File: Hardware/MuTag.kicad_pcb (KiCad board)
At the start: 2 copper layers, 30 x 20 mm, 32 parts, among them IC1 ST25DV04K-IER6S3, J1 Conn_01x02, J2 Conn_01x04, J3 Conn_01x06, U1 STM8

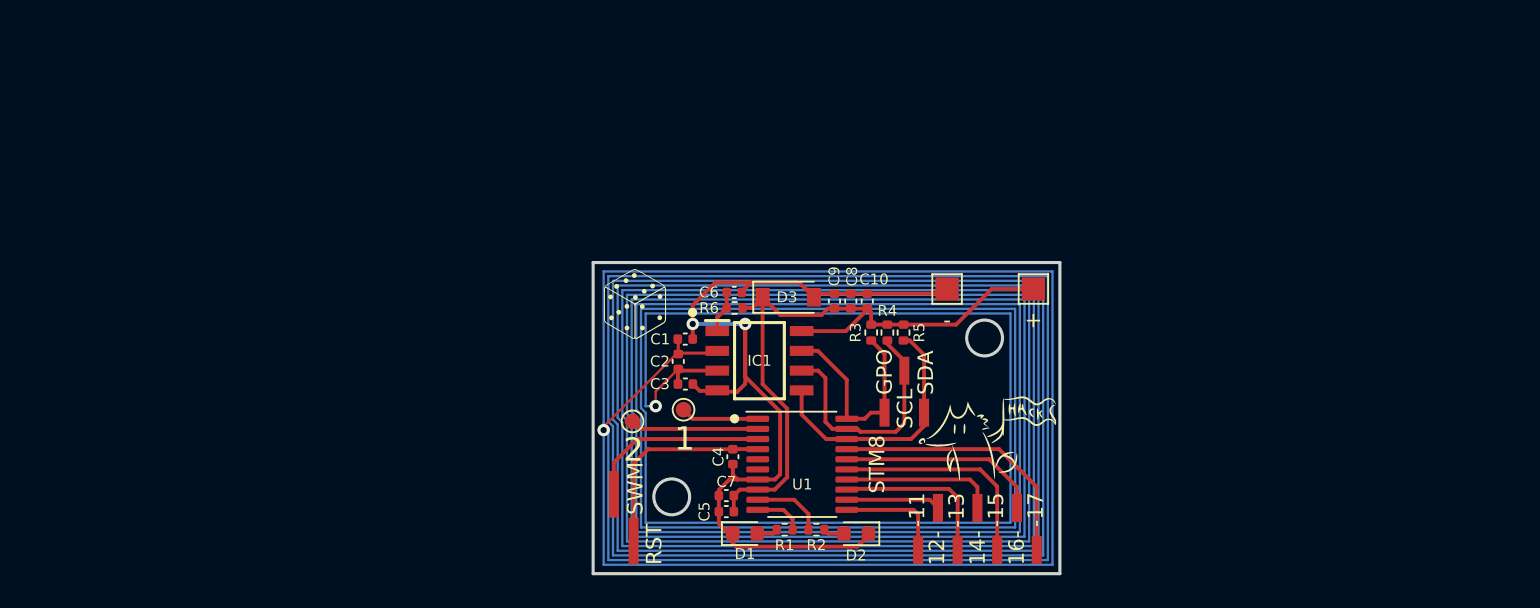
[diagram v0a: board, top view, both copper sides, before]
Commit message: First routing of new version - no antenna
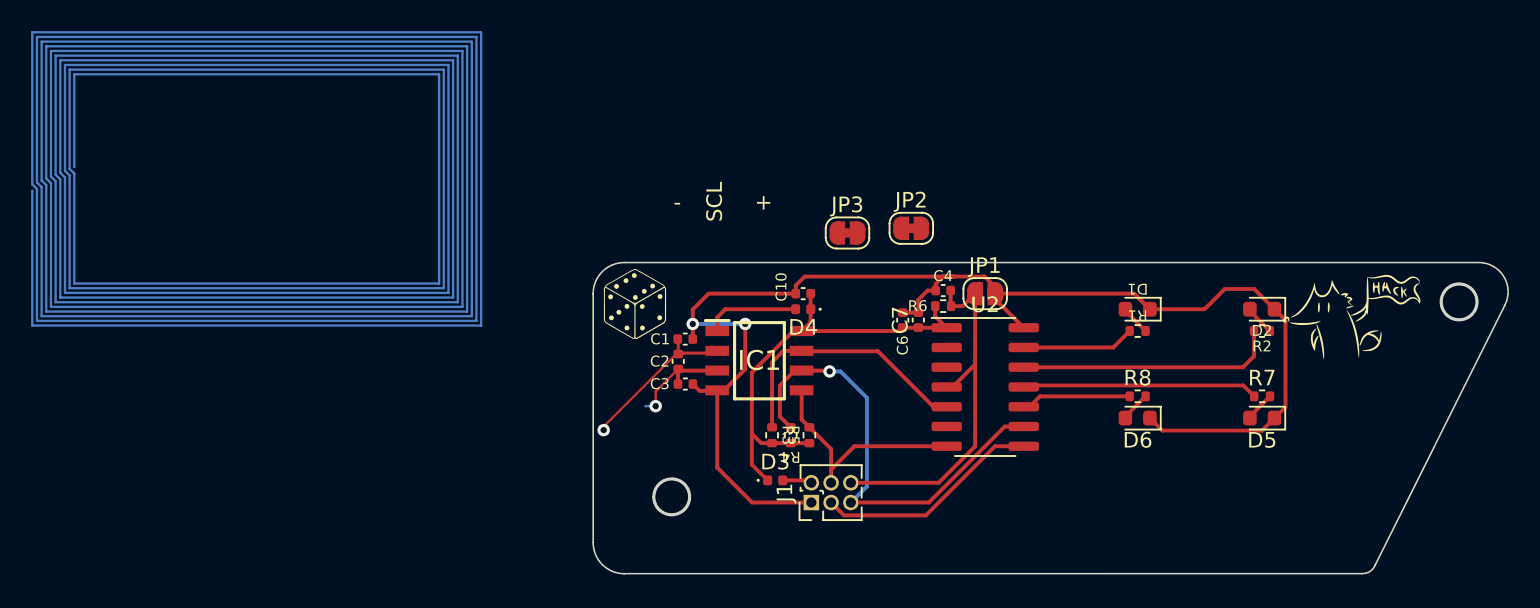
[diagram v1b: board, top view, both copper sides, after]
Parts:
- removed C5: 1uF, Capacitor_SMD:C_0402_1005Metric
- removed C8: 4.7uF, Capacitor_SMD:C_0402_1005Metric
- removed C9: 100nF, Capacitor_SMD:C_0402_1005Metric
- removed J2: Conn_01x04, Connector_PinHeader_1.27mm:PinHeader_1x02_P1.27mm_Vertical_SMD_Pin1Right
- removed J3: Conn_01x06, Connector_PinSocket_1.27mm:PinSocket_1x07_P1.27mm_Vertical_SMD_Pin1Right
- removed TP1, TP2: TestPoint, TestPoint:TestPoint_Pad_1.5x1.5mm
- removed TP3, TP4: TestPoint, TestPoint:TestPoint_Pad_D1.0mm
- removed U1: STM8, Package_SO:TSSOP-20_4.4x6.5mm_P0.65mm
- added D4: D, Diode_SMD:D_0402_1005Metric, F.Cu at (43.5, 23.0)
- added D5: LED, LED_SMD:LED_0603_1608Metric, F.Cu at (73.0, 30.0)
- added D6: LED, LED_SMD:LED_0603_1608Metric, F.Cu at (65.0, 30.0)
- added JP1: RESET_JMP, Jumper:SolderJumper-2_P1.3mm_Open_RoundedPad1.0x1.5mm, F.Cu at (55.2, 22.0)
- added JP2: SCL_JMP, Jumper:SolderJumper-2_P1.3mm_Bridged_RoundedPad1.0x1.5mm, F.Cu at (50.5, 17.8)
- added JP3: SDA_JMP, Jumper:SolderJumper-2_P1.3mm_Bridged_RoundedPad1.0x1.5mm, F.Cu at (46.4, 18.1)
- added R7: 220, Resistor_SMD:R_0402_1005Metric, F.Cu at (73.0, 28.6)
- added R8: 220, Resistor_SMD:R_0402_1005Metric, F.Cu at (65.0, 28.6)
- added U2: ATtiny24A-SS, Package_SO:SOIC-14_3.9x8.7mm_P1.27mm, F.Cu at (55.2, 28.0)
- C6: value 10nF -> 100nF
- C7: value 100nF -> 1nF
- D3: value D_Zener -> D; footprint Diode_SMD:D_SOD-123 -> Diode_SMD:D_0402_1005Metric
- J1: value Conn_01x02 -> SPI_Header; footprint Connector_PinSocket_1.27mm:PinSocket_1x03_P1.27mm_Vertical_SMD_Pin1Right -> Connector_PinHeader_1.27mm:PinHeader_2x03_P1.27mm_Vertical
- R1, R2: value 1.5K -> 220
- R3: value 20K -> 1.5K
- R6: value 200 -> 4.7K
- moved A1 39.8 mm to (22.9, 24.1)
- moved R2 31.4 mm to (73.0, 24.4)
- moved D2 29.8 mm to (73.0, 23.0)
- moved D1 29.1 mm to (65.0, 23.0), turned to 180 degrees
- moved R1 26.0 mm to (65.0, 24.4), turned to 180 degrees
- moved G*** 24.7 mm to (78.8, 23.5)
- moved C4 17.2 mm to (52.5, 21.8), turned to 180 degrees
- moved C7 16.7 mm to (50.9, 23.7), turned to 90 degrees
- moved G*** 15.0 mm to (60.0, 30.0)
- moved R6 13.4 mm to (52.5, 22.8)
- moved D3 11.8 mm to (41.7, 34.0)
- moved C6 11.0 mm to (49.9, 23.7), turned to 90 degrees
- moved J1 9.30 mm to (44.0, 35.4), turned to 90 degrees
- moved R3 9.17 mm to (41.5, 31.1), turned to 90 degrees
- moved R4 9.06 mm to (42.7, 31.1), turned to 90 degrees
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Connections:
- C4 pad 1: /MCU_RESET -> /RESET
- C6 pad 1: /NFC_V_EH -> VCC
- D3 pad 2: GND -> VDD
- IC1 pad 5: /NFC_SDA -> /SDA/MOSI
- IC1 pad 6: /NFC_SCL -> /SCL/SCK
- IC1 pad 7: /NFC_GPO -> /INT0
- J1 pad 1: /NFC_SDA -> GND
- J1 pad 2: /NFC_SCL -> VDD
- J1 pad 3: /NFC_GPO -> /MISO
- R2 pad 1: /LED_BLU -> /LED_BLUE
- R3 pad 2: /NFC_GPO -> /INT0
- R4 pad 2: /NFC_SCL -> /SCL/SCK
- R5 pad 2: /NFC_SDA -> /SDA/MOSI
- R6 pad 1: /NFC_V_EH -> VCC
- R6 pad 2: VCC -> /RESET
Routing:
- net /SCL/SCK: track 0.00 -> 30.0 mm, vias 0 -> 1
- net GND: track 60.8 -> 90.2 mm
- net /RESET: track 0.00 -> 24.4 mm
- net Net-(U1-Pad17): track 17.3 -> 0.00 mm
- net /INT0: track 0.00 -> 17.2 mm
- net /LED_BLUE: track 0.00 -> 16.7 mm
- net /NFC_SDA: track 16.7 -> 0.00 mm
- net /NFC_SCL: track 15.9 -> 0.00 mm
- net /LED_GREEN: track 0.00 -> 15.1 mm
- net /SDA/MOSI: track 0.00 -> 15.1 mm
- net /MISO: track 0.00 -> 14.6 mm
- net Net-(U1-Pad15): track 14.2 -> 0.00 mm
- net VCC: track 43.5 -> 29.4 mm
- net /NFC_GPO: track 13.8 -> 0.00 mm
- net /MCU_RESET: track 13.3 -> 0.00 mm
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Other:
- board size 30 x 20 mm -> 58.8 x 20 mm
- board text removed: "-11"
- board text removed: "-13"
- board text removed: "-15"
- board text removed: "-17"
- board text removed: "1"
- board text removed: "12-"
- board text removed: "14-"
- board text removed: "16-"
- board text removed: "2"
- board text removed: "GPO"
- board text removed: "RST"
- board text removed: "SDA"
- board text removed: "SWM"

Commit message: New finished routing, with bigger antenna and leds - ready for production
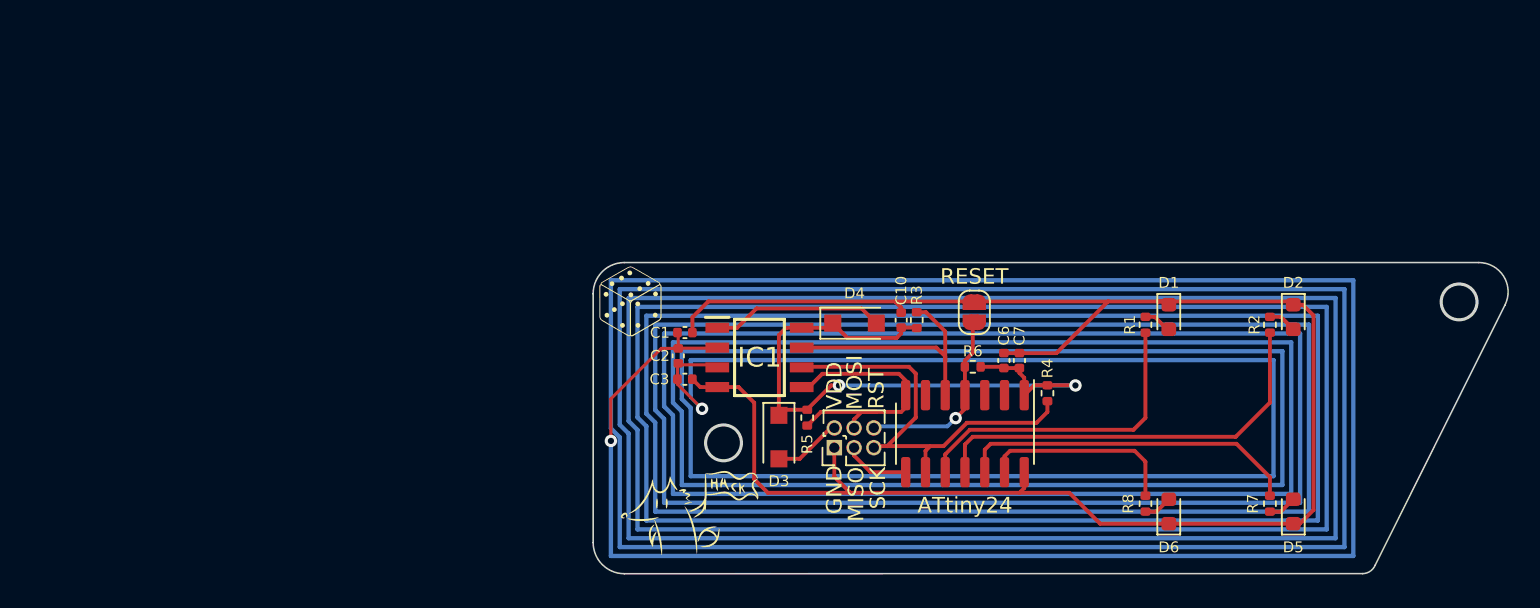
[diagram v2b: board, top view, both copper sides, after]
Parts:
- removed C4: 100nF, Capacitor_SMD:C_0402_1005Metric
- removed JP2: SCL_JMP, Jumper:SolderJumper-2_P1.3mm_Bridged_RoundedPad1.0x1.5mm
- removed JP3: SDA_JMP, Jumper:SolderJumper-2_P1.3mm_Bridged_RoundedPad1.0x1.5mm
- added G***: LOGO, LOGO, B.Cu at (42.5, 30.0)
- A1: footprint MuTag Antenna:mutag_antenna -> MuTag Antenna:mutag_new_antenna
- D1: value LED -> LED_RED
- D2: value LED -> LED_BLUE
- D3, D4: footprint Diode_SMD:D_0402_1005Metric -> Diode_SMD:D_SOD-123F
- D5: value LED -> LED_GREEN
- D6: value LED -> LED_YELLOW
- JP1: value RESET_JMP -> RESET
- R6: value 4.7K -> 10K
- U2: value ATtiny24A-SS -> ATtiny24
- moved A1 58.1 mm to (79.0, 39.0)
- moved G*** 44.4 mm to (36.2, 36.1)
- moved R4 16.7 mm to (59.2, 28.4), turned to -90 degrees
- moved R3 11.9 mm to (50.8, 23.7)
- moved C6 7.00 mm to (56.4, 26.3)
- moved C7 7.00 mm to (57.4, 26.3)
- moved R7 6.92 mm to (73.5, 35.5), turned to -90 degrees
- moved R8 6.92 mm to (65.5, 35.5), turned to -90 degrees
- moved C10 6.53 mm to (49.8, 23.7), turned to 90 degrees
- moved D5 6.32 mm to (75.0, 36.0), turned to 90 degrees
- moved D6 6.32 mm to (67.0, 36.0), turned to 90 degrees
- moved G*** 5.00 mm to (65.0, 30.0)
- moved R6 4.34 mm to (54.4, 26.7), turned to 180 degrees
- moved J1 3.82 mm to (45.5, 31.9)
- moved D4 3.42 mm to (46.8, 23.9), turned to 0 degrees
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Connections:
- U2 pad 10: /LED_YELLOW -> /LED_RED
- U2 pad 11: /LED_GREEN -> /LED_BLUE
- U2 pad 12: /LED_BLUE -> /LED_GREEN
- U2 pad 13: /LED_RED -> /LED_YELLOW
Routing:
- net GND: track 90.2 -> 115.7 mm, vias 2 -> 0
- net VCC: track 29.4 -> 43.1 mm, vias 0 -> 2
- net /LED_RED: track 7.45 -> 20.5 mm
- net /RESET: track 24.4 -> 12.0 mm, vias 0 -> 1
- net /LED_BLUE: track 16.7 -> 27.0 mm
- net /MISO: track 14.6 -> 4.27 mm
- net /LED_GREEN: track 15.1 -> 22.0 mm
- net /LED_YELLOW: track 7.09 -> 12.7 mm
- net /NFC_V_EH: track 6.14 -> 11.1 mm
- net /SCL/SCK: track 30.0 -> 27.0 mm, vias 1 -> 0
- net VDD: track 1.90 -> 4.64 mm
- net /SDA/MOSI: track 15.1 -> 17.5 mm
- net Net-(A1-Pad1): track 10.5 -> 11.9 mm
- net /INT0: track 17.2 -> 16.4 mm
- net Net-(A1-Pad2): track 7.17 -> 7.74 mm
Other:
- outline, holes or cut-outs redrawn
- board text added: "GND"
- board text added: "MISO"
- board text added: "MOSI"
- board text added: "RST"
- board text added: "SCK"
- board text added: "VDD"
- board text removed: "+"
- board text removed: "-"
- board text removed: "SCL"

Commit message: Ordered Version v2
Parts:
- removed the G*** at (42.5, 30.0)
- removed the G*** at (65.0, 30.0)
- added G***: LOGO, LOGO, F.Cu at (70.8, 29.7)
- added G***: LOGO, LOGO, B.Cu at (55.6, 30.1)

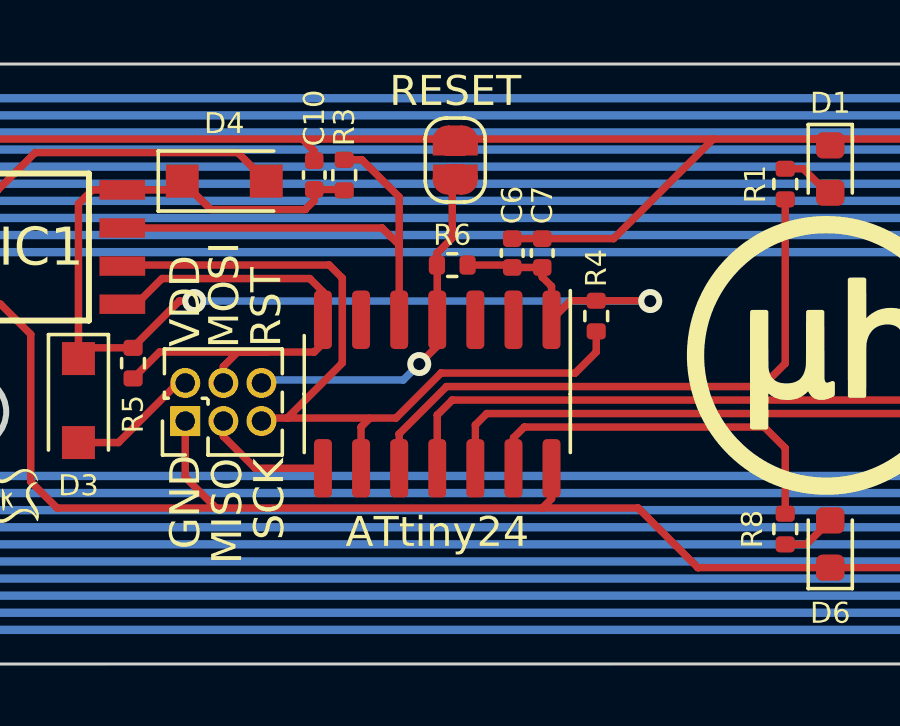
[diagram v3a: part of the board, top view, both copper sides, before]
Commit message: Second version first commit - produced and tested: all working
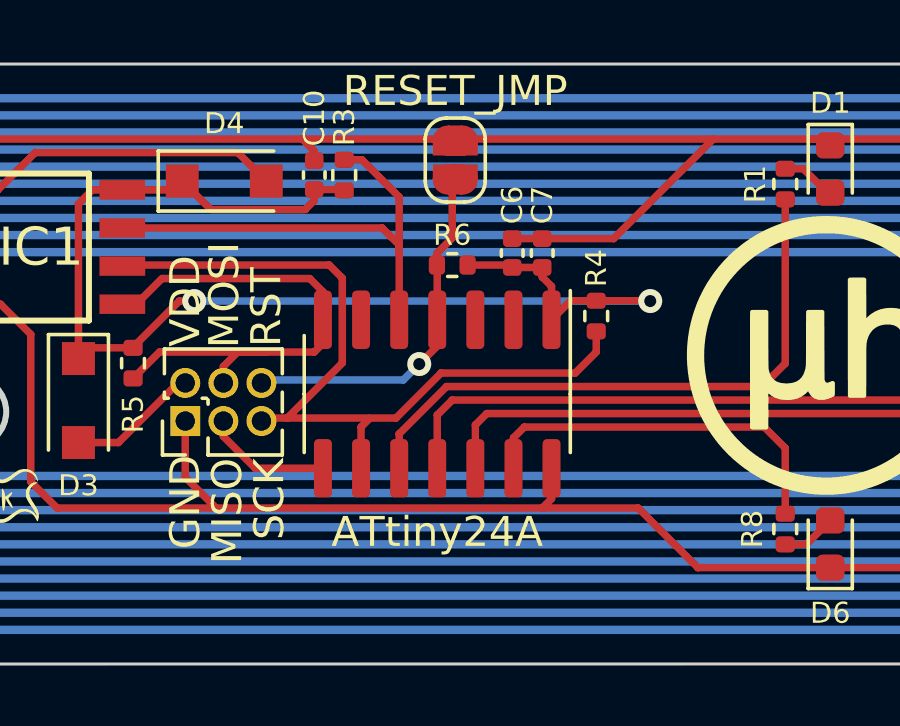
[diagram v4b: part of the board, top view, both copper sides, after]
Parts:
- JP1: value RESET -> RESET_JMP
- U2: value ATtiny24 -> ATtiny24A

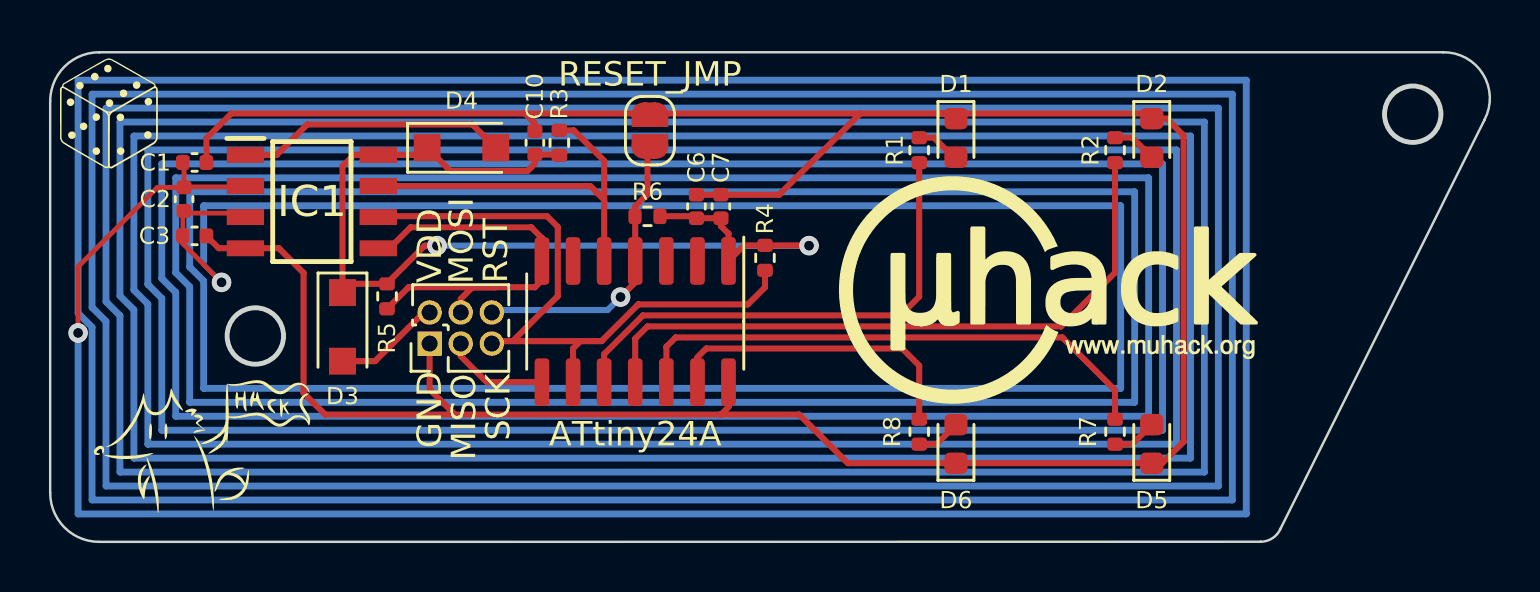
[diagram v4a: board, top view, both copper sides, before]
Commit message: Version v2.1 - Set production and docs with ATTiny44a, removed diode from VCC port, moved components to fit bigger port, led resistors value changed to 160
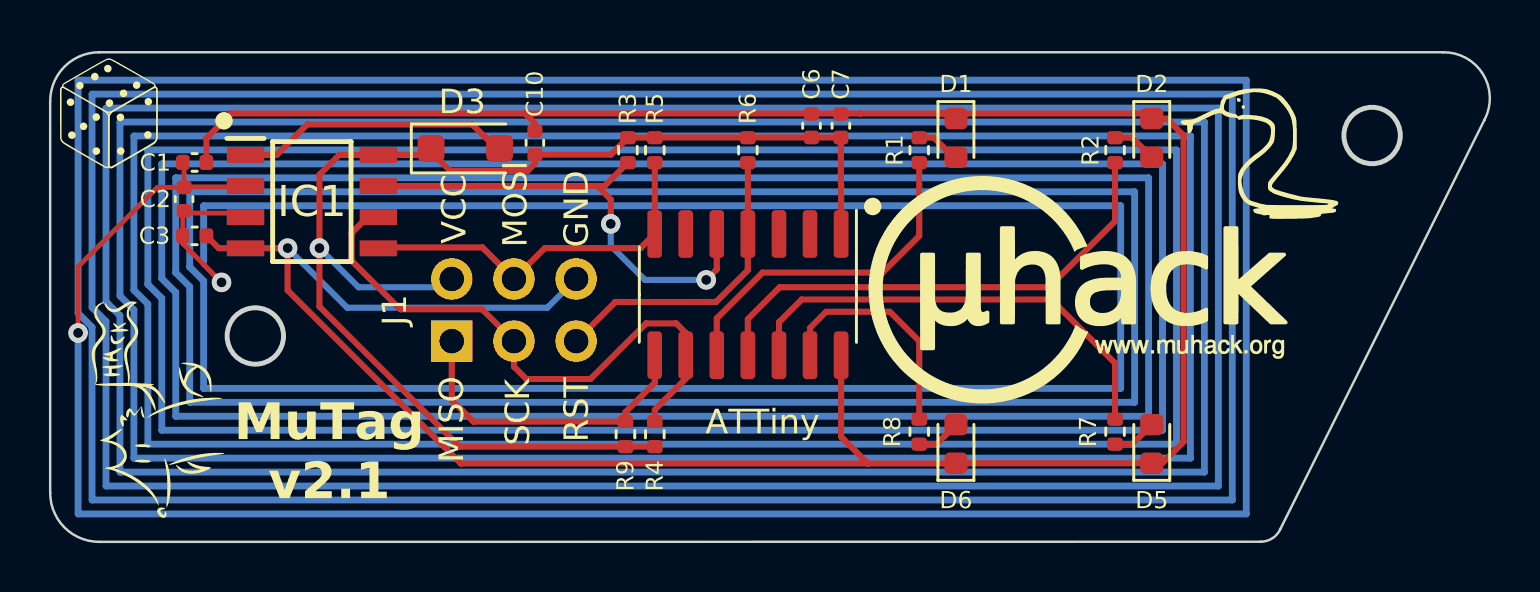
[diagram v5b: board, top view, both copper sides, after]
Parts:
- removed D4: D, Diode_SMD:D_SOD-123F
- removed the G*** at (55.6, 30.1)
- removed JP1: RESET_JMP, Jumper:SolderJumper-2_P1.3mm_Open_RoundedPad1.0x1.5mm
- added G***: LOGO, LOGO, F.Cu at (80.3, 23.9)
- added G***: LOGO, LOGO, B.Cu at (70.2, 29.8)
- added G***: LOGO, LOGO, B.Cu at (49.9, 30.2)
- added R9: 1.5K, Resistor_SMD:R_0402_1005Metric, F.Cu at (53.5, 35.6)
- J1: footprint Connector_PinHeader_1.27mm:PinHeader_2x03_P1.27mm_Vertical -> Connector_PinHeader_2.54mm:PinHeader_2x03_P2.54mm_Vertical
- R1, R2, R7, R8: value 220 -> 160
- U2: value ATtiny24A -> ATTiny
- moved R5 12.5 mm to (54.7, 24.0)
- moved D3 8.85 mm to (47.0, 23.9), turned to 0 degrees
- moved R4 8.49 mm to (54.7, 35.6), turned to 90 degrees
- moved C7 5.91 mm to (62.3, 23.0)
- moved C6 5.74 mm to (61.1, 23.0)
- moved R6 4.91 mm to (58.5, 24.0), turned to -90 degrees
- moved U2 4.73 mm to (58.5, 29.9)
- moved R3 2.82 mm to (53.6, 24.0), turned to -90 degrees
- moved G*** 2.34 mm to (34.4, 34.6), turned to 90 degrees
- moved G*** 1.21 mm to (72.0, 29.7)
- moved J1 0.91 mm to (46.4, 31.8)
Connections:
- D3 pad 2: VDD -> /NFC_V_EH
- J1 pad 1: GND -> /MISO
- J1 pad 2: VDD -> VCC
- J1 pad 3: /MISO -> /SCL/SCK
- J1 pad 5: /SCL/SCK -> /RESET
- J1 pad 6: /RESET -> GND
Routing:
- net VCC: track 43.1 -> 54.6 mm, vias 2 -> 1
- net /MISO: track 4.27 -> 13.1 mm
- net /LED_BLUE: track 27.0 -> 20.5 mm
- net /LED_RED: track 20.5 -> 14.2 mm
- net VDD: track 4.64 -> 0.00 mm
- net /INT0: track 16.4 -> 20.4 mm, vias 0 -> 2
- net GND: track 115.7 -> 119.1 mm, vias 0 -> 1
- net /LED_GREEN: track 22.0 -> 18.8 mm
- net /LED_YELLOW: track 12.7 -> 9.54 mm
- net /SCL/SCK: track 27.0 -> 24.0 mm
- net /SDA/MOSI: track 17.5 -> 15.5 mm
- net /RESET: track 12.0 -> 12.6 mm, vias 1 -> 0
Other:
- outline, holes or cut-outs redrawn
- board text added: "MuTag v2.1"
- board text added: "VCC"
- board text removed: "VDD"
